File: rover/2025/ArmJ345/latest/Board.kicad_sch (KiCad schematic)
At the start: 0 parts

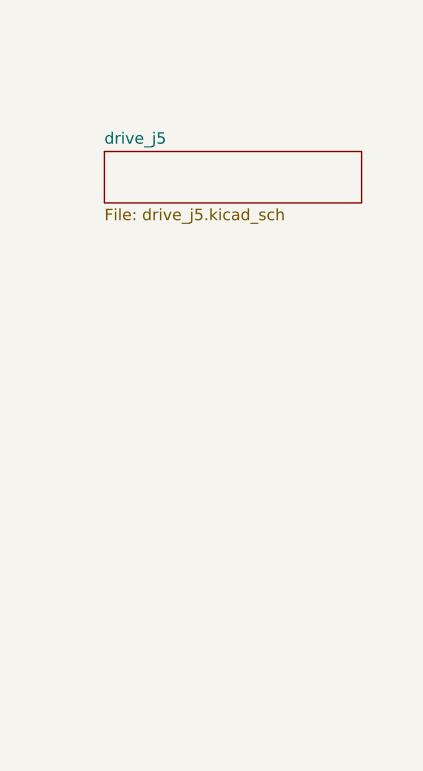
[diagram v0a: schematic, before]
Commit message: ArmJ345 routing
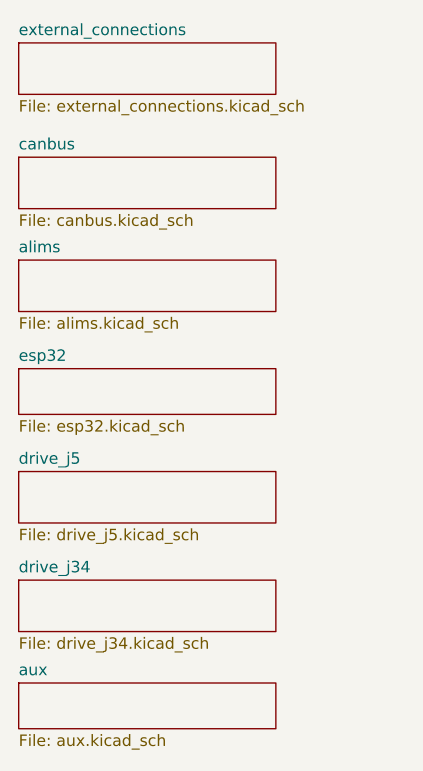
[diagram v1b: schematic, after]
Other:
- added sheet alims (alims.kicad_sch)
- added sheet aux (aux.kicad_sch)
- added sheet canbus (canbus.kicad_sch)
- added sheet drive_j34 (drive_j34.kicad_sch)
- added sheet esp32 (esp32.kicad_sch)
- added sheet external_connections (external_connections.kicad_sch)
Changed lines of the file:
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@@
 	)
 	(sheet
-		(at 34.925 31.115)
+		(at 25.4 55.245)
+		(size 28.575 5.08)
+		(fields_autoplaced yes)
+		(stroke
+			(width 0.1524)
+			(type solid)
+		)
+		(fill
+			(color 0 0 0 0.0000)
+		)
+		(property "Sheetname" "esp32"
+			(at 25.4 54.5334 0)
+			(effects
+				(font
+					(size 1.27 1.27)
+				)
+				(justify left bottom)
+			)
+		)
+		(property "Sheetfile" "esp32.kicad_sch"
+			(at 25.4 60.9096 0)
+			(effects
+				(font
+					(size 1.27 1.27)
+				)
+				(justify left top)
+			)
+		)
+		(instances
+			(project "ArmJ345"
+				(path "/a4fa9b30-7b48-474a-bdaa-0d7a6d26a697/8da6c8a9-d96a-428b-ac41-906630b726a3"
+					(page "3")
+				)
+			)
+		)
+	)
+	(sheet
+		(at 25.4 78.74)
+		(size 28.575 5.715)
+		(fields_autoplaced yes)
+		(stroke
+			(width 0.1524)
+			(type solid)
+		)
+		(fill
+			(color 0 0 0 0.0000)
+		)
+		(property "Sheetname" "drive_j34"
+			(at 25.4 78.0284 0)
+			(effects
+				(font
+					(size 1.27 1.27)
+				)
+				(justify left bottom)
+			)
+		)
+		(property "Sheetfile" "drive_j34.kicad_sch"
+			(at 25.4 85.0396 0)
+			(effects
+				(font
+					(size 1.27 1.27)
+				)
+				(justify left top)
+			)
+		)
+		(instances
+			(project "ArmJ345"
+				(path "/a4fa9b30-7b48-474a-bdaa-0d7a6d26a697/8da6c8a9-d96a-428b-ac41-906630b726a3"
+					(page "8")
+				)
+			)
+		)
+	)
+	(sheet
+		(at 25.4 43.18)
+		(size 28.575 5.715)
+		(fields_autoplaced yes)
+		(stroke
+			(width 0.1524)
+			(type solid)
+		)
+		(fill
+			(color 0 0 0 0.0000)
+		)
+		(property "Sheetname" "alims"
+			(at 25.4 42.4684 0)
+			(effects
+				(font
+					(size 1.27 1.27)
+				)
+				(justify left bottom)
+			)
+		)
+		(property "Sheetfile" "alims.kicad_sch"
+			(at 25.4 49.4796 0)
+			(effects
+				(font
+					(size 1.27 1.27)
+				)
+				(justify left top)
+			)
+		)
+		(instances
+			(project "ArmJ345"
+				(path "/a4fa9b30-7b48-474a-bdaa-0d7a6d26a697/8da6c8a9-d96a-428b-ac41-906630b726a3"
+					(page "6")
+				)
+			)
+		)
+	)
+	(sheet
+		(at 25.4 19.05)
+		(size 28.575 5.715)
+		(fields_autoplaced yes)
+		(stroke
+			(width 0.1524)
+			(type solid)
+		)
+		(fill
+			(color 0 0 0 0.0000)
+		)
+		(property "Sheetname" "external_connections"
+			(at 25.4 18.3384 0)
+			(effects
+				(font
+					(size 1.27 1.27)
+				)
+				(justify left bottom)
+			)
+		)
+		(property "Sheetfile" "external_connections.kicad_sch"
+			(at 25.4 25.3496 0)
+			(effects
+				(font
+					(size 1.27 1.27)
+				)
+				(justify left top)
+			)
+		)
+		(instances
+			(project "ArmJ345"
+				(path "/a4fa9b30-7b48-474a-bdaa-0d7a6d26a697/8da6c8a9-d96a-428b-ac41-906630b726a3"
+					(page "4")
+				)
+			)
+		)
+	)
+	(sheet
+		(at 25.4 90.17)
+		(size 28.575 5.08)
+		(fields_autoplaced yes)
+		(stroke
+			(width 0.1524)
+			(type solid)
+		)
+		(fill
+			(color 0 0 0 0.0000)
+		)
+		(property "Sheetname" "aux"
+			(at 25.4 89.4584 0)
+			(effects
+				(font
+					(size 1.27 1.27)
+				)
+				(justify left bottom)
+			)
+		)
+		(property "Sheetfile" "aux.kicad_sch"
+			(at 25.4 95.8346 0)
+			(effects
+				(font
+					(size 1.27 1.27)
+				)
+				(justify left top)
+			)
+		)
+		(instances
+			(project "ArmJ345"
+				(path "/a4fa9b30-7b48-474a-bdaa-0d7a6d26a697/8da6c8a9-d96a-428b-ac41-906630b726a3"
+					(page "9")
+				)
+			)
+		)
+	)
+	(sheet
+		(at 25.4 66.675)
 		(size 28.575 5.715)
 		(fields_autoplaced yes)
@@
 		)
 		(property "Sheetname" "drive_j5"
-			(at 34.925 30.4034 0)
+			(at 25.4 65.9634 0)
 			(effects
 				(font
@@
 		)
 		(property "Sheetfile" "drive_j5.kicad_sch"
-			(at 34.925 37.4146 0)
-			(effects
-				(font
-					(size 1.27 1.27)
-				)
-				(justify left top)
-			)
-		)
-		(instances
-			(project "ArmJ345"
-				(path "/a4fa9b30-7b48-474a-bdaa-0d7a6d26a697/8da6c8a9-d96a-428b-ac41-906630b726a3"
-					(page "3")
-				)
-			)
+			(at 25.4 72.9746 0)
+			(effects
+				(font
+					(size 1.27 1.27)
+				)
+				(justify left top)
+			)
+		)
+		(instances
+			(project "ArmJ345"
+				(path "/a4fa9b30-7b48-474a-bdaa-0d7a6d26a697/8da6c8a9-d96a-428b-ac41-906630b726a3"
+					(page "7")
+				)
+			)
+		)
+	)
+	(sheet
+		(at 25.4 31.75)
+		(size 28.575 5.715)
+		(fields_autoplaced yes)
+		(stroke
+			(width 0.1524)
+			(type solid)
+		)
+		(fill
+			(color 0 0 0 0.0000)
+		)
+		(property "Sheetname" "canbus"
+			(at 25.4 31.0384 0)
+			(effects
+				(font
+					(size 1.27 1.27)
+				)
+				(justify left bottom)
+			)
+		)
+		(property "Sheetfile" "canbus.kicad_sch"
+			(at 25.4 38.0496 0)
+			(effects
+				(font
+					(size 1.27 1.27)
+				)
+				(justify left top)
+			)
+		)
+		(instances
+			(project "ArmJ345"
+				(path "/a4fa9b30-7b48-474a-bdaa-0d7a6d26a697/8da6c8a9-d96a-428b-ac41-906630b726a3"
+					(page "5")
+				)
+			)
